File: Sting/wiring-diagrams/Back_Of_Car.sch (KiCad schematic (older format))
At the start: 34 parts, among them M1 Starter Motor, SW3 ExternalKill

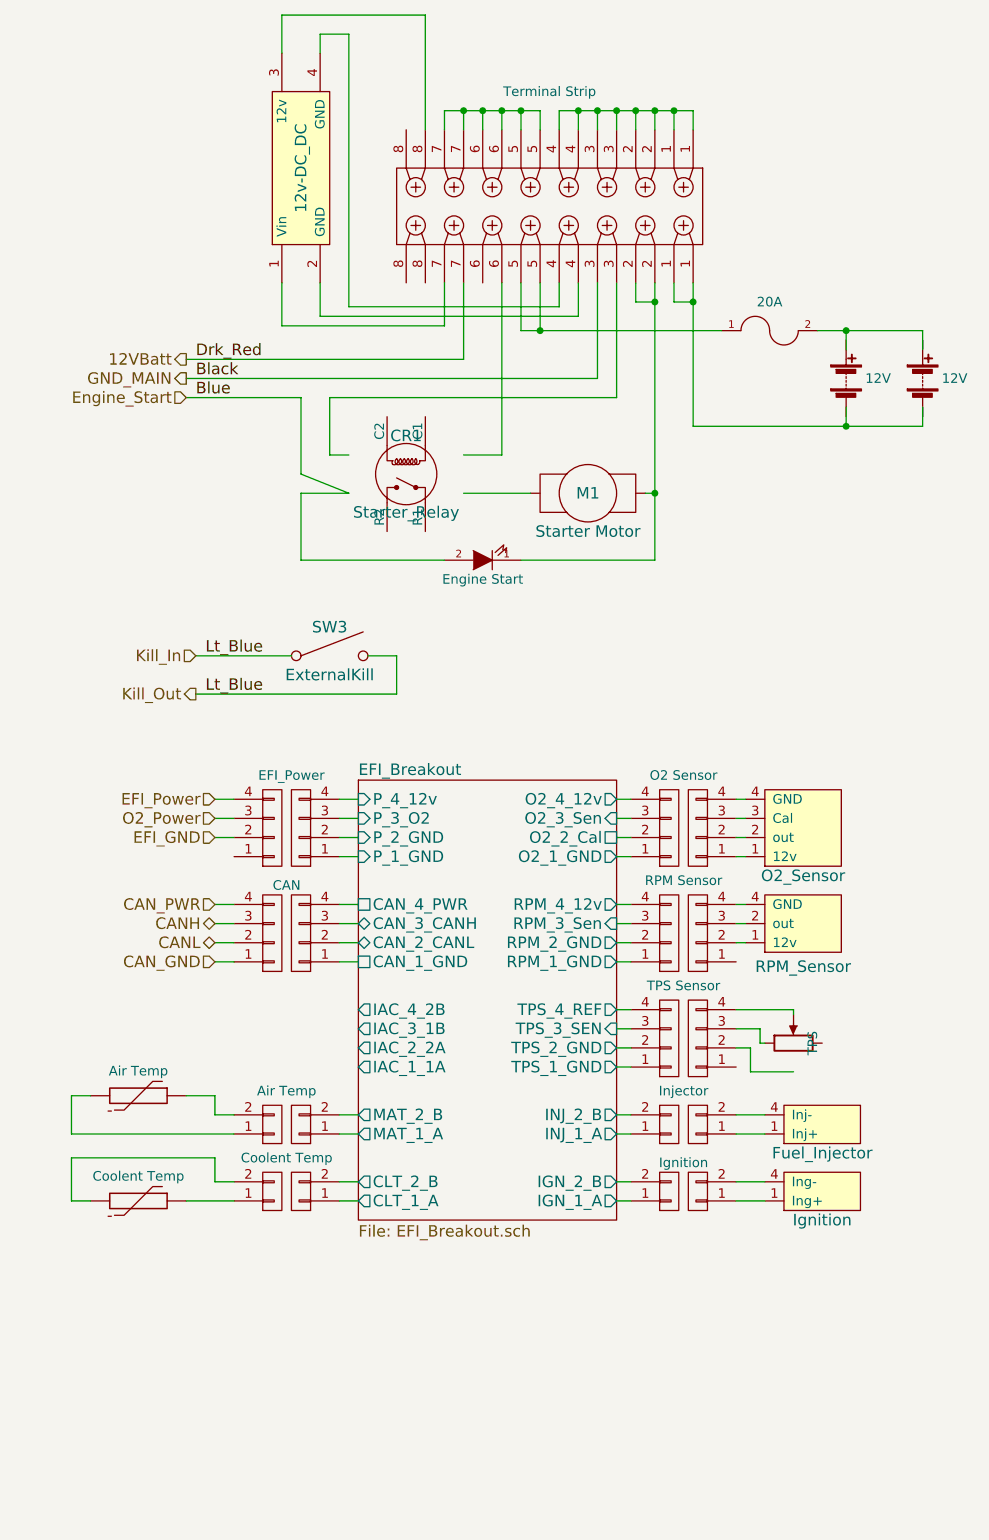
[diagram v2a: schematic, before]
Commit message: fixed missing parts updated sensor boards
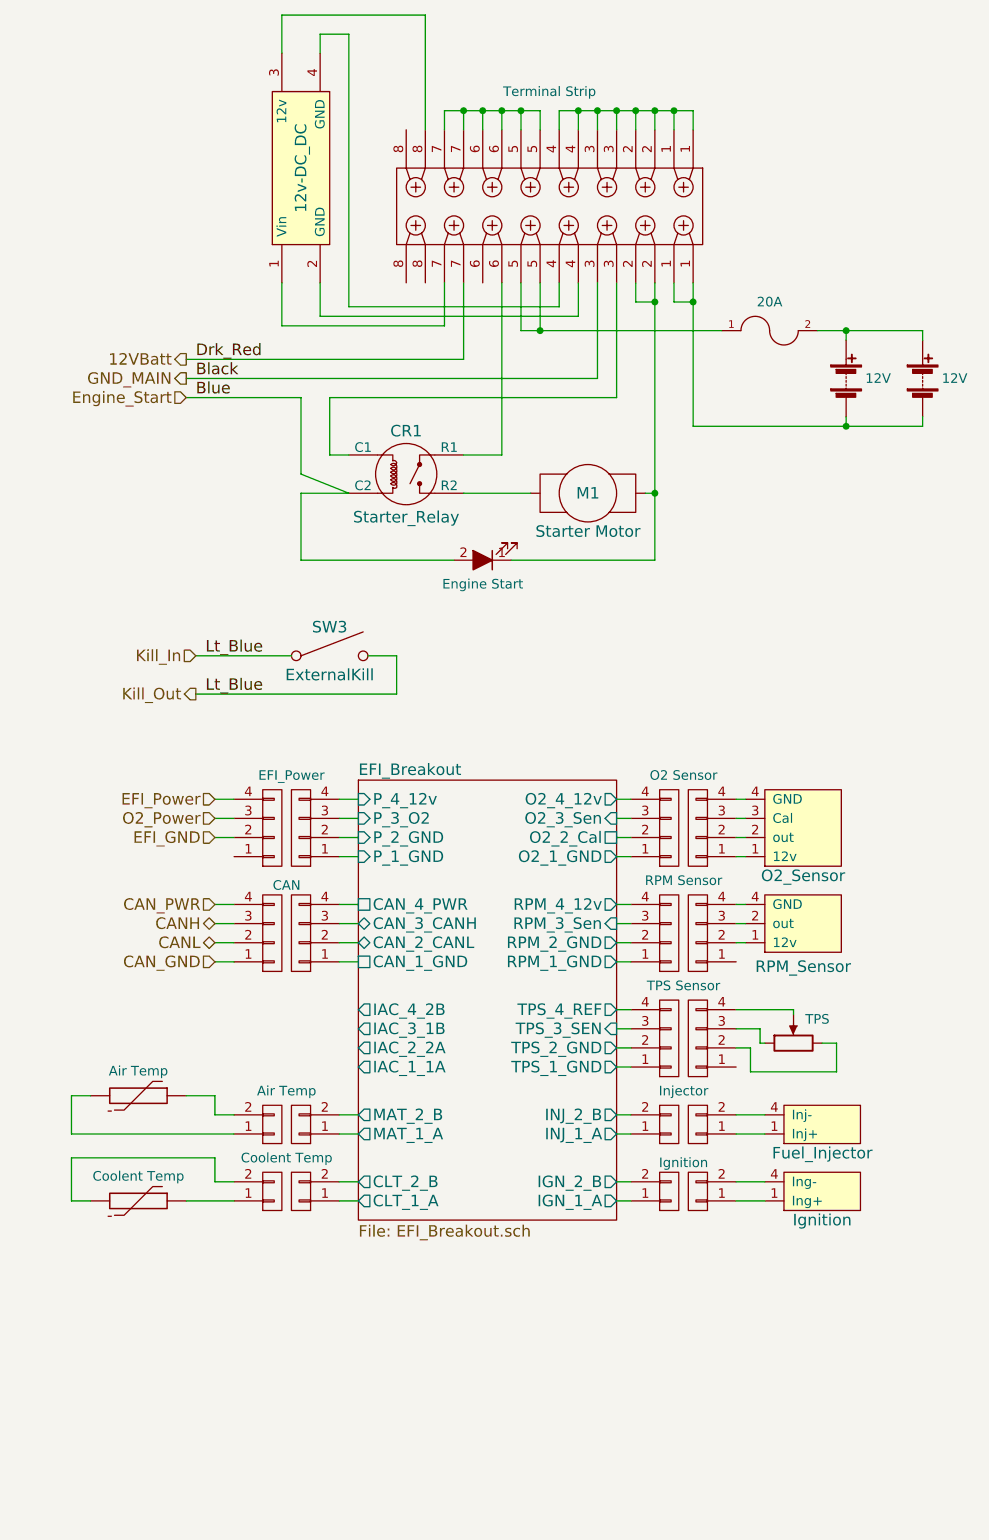
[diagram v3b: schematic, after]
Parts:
- removed D?: Engine Start, symbol LED
- added D?: Engine Start, symbol LED_ALT
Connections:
- wire segments 134 -> 152
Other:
- moved on the sheet: CR1
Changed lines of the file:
@@
 U 1 1 57E6F37B
 P 3975 3925
-F 0 "CR1" V 3775 3925 60  0000 C CNN
-F 1 "Starter_Relay" V 4175 3925 60  0000 C CNN
+F 0 "CR1" H 3975 4150 60  0000 C CNN
+F 1 "Starter_Relay" H 3975 3700 60  0000 C CNN
 F 2 "" H 3975 3925 60  0001 C CNN
 F 3 "" H 3975 3925 60  0001 C CNN
 	1    3975 3925
-	0    1    1    0
+	1    0    0    -1
 $EndComp
 Text HLabel 2825 3425 0    60   Output ~ 0
@@
 Text HLabel 2825 3325 0    60   Output ~ 0
 12VBatt
-$Comp
-L LED D?
-U 1 1 57E7BBBA
-P 4375 4375
-F 0 "D?" H 4375 4475 50  0001 C CNN
-F 1 "Engine Start" H 4375 4475 50  0000 C CNN
-F 2 "" H 4375 4375 50  0000 C CNN
-F 3 "" H 4375 4375 50  0000 C CNN
-	1    4375 4375
-	-1   0    0    1
-$EndComp
 Text HLabel 2825 3525 0    60   Input ~ 0
 Engine_Start
@@
 U 1 1 57E6F190
 P 6275 3425
+AR Path="/57E6F190" Ref="BT?"  Part="1"
+AR Path="/57E2AF30/57E6F190" Ref="BT?"  Part="1"
 F 0 "BT?" V 6075 3375 50  0001 L CNN
 F 1 "12V" H 6375 3425 50  0000 L CNN
@@
 U 1 1 5880064A
 P 6675 3425
+AR Path="/5880064A" Ref="BT?"  Part="1"
+AR Path="/57E2AF30/5880064A" Ref="BT?"  Part="1"
 F 0 "BT?" V 6475 3375 50  0001 L CNN
 F 1 "12V" H 6775 3425 50  0000 L CNN
@@
 U 1 1 5893DA3D
 P 6000 6900
-F 0 "TPS" H 6000 6800 50  0000 C CNN
+AR Path="/5893DA3D" Ref="TPS"  Part="1"
+AR Path="/57E2AF30/5893DA3D" Ref="TPS"  Part="1"
+F 0 "TPS" V 6125 6775 50  0000 C CNN
 F 1 "POT" H 6000 6900 50  0001 C CNN
 F 2 "" H 6000 6900 50  0000 C CNN
@@
 	5475 2025 5475 2125
 Wire Wire Line
-	4775 2025 5475 2025
+	4775 2025 4875 2025
+Wire Wire Line
+	4875 2025 4975 2025
+Wire Wire Line
+	4975 2025 5075 2025
+Wire Wire Line
+	5075 2025 5175 2025
+Wire Wire Line
+	5175 2025 5275 2025
+Wire Wire Line
+	5275 2025 5375 2025
+Wire Wire Line
+	5375 2025 5475 2025
 Wire Wire Line
 	5375 2025 5375 2125
@@
 Connection ~ 4475 2025
 Wire Wire Line
-	5475 3675 6675 3675
-Wire Wire Line
-	5475 2925 5475 3675
+	5475 3675 6275 3675
+Wire Wire Line
+	6275 3675 6675 3675
+Wire Wire Line
+	5475 2925 5475 3025
+Wire Wire Line
+	5475 3025 5475 3675
 Wire Wire Line
 	5375 2925 5375 3025
@@
 	2825 3525 3425 3525
 Wire Wire Line
-	5275 2925 5275 4375
+	5275 2925 5275 3025
+Wire Wire Line
+	5275 3025 5275 4025
+Wire Wire Line
+	5275 4025 5275 4375
 Wire Wire Line
 	5175 2925 5175 3025
@@
 	4675 3175 4675 2925
 Wire Wire Line
-	4175 2025 4675 2025
+	4175 2025 4275 2025
+Wire Wire Line
+	4275 2025 4375 2025
+Wire Wire Line
+	4375 2025 4475 2025
+Wire Wire Line
+	4475 2025 4575 2025
+Wire Wire Line
+	4575 2025 4675 2025
 Wire Wire Line
 	4775 2125 4775 2025
@@
 	5275 4025 5225 4025
 Wire Wire Line
-	4175 4375 3425 4375
+	4225 4375 3425 4375
 Wire Wire Line
 	3425 4375 3425 4025
@@
 	3425 4025 3675 4025
 Wire Wire Line
-	5275 4375 4575 4375
+	5275 4375 4525 4375
 Connection ~ 5275 4025
 Wire Wire Line
@@
 	3575 3825 3675 3825
 Wire Wire Line
-	6125 3175 6675 3175
-Wire Wire Line
-	4575 3175 5625 3175
-Wire Wire Line
-	6275 3675 6275 3575
-Wire Wire Line
-	6275 3275 6275 3175
-Wire Wire Line
-	6675 3175 6675 3275
+	6125 3175 6275 3175
+Wire Wire Line
+	6275 3175 6675 3175
+Wire Wire Line
+	4575 3175 4675 3175
+Wire Wire Line
+	4675 3175 5625 3175
+Wire Wire Line
+	6275 3675 6275 3625
+Wire Wire Line
+	6275 3225 6275 3175
+Wire Wire Line
+	6675 3175 6675 3225
 Connection ~ 6275 3175
 Wire Wire Line
-	6675 3675 6675 3575
+	6675 3675 6675 3625
 Connection ~ 6275 3675
 Wire Wire Line
@@
 	6000 6725 5700 6725
 Wire Wire Line
-	6000 7050 5775 7050
+	6225 7050 5775 7050
 Wire Wire Line
 	5775 7050 5775 6925
@@
 Wire Wire Line
 	4075 1525 4075 2125
+Wire Wire Line
+	6225 7050 6225 6900
+Wire Wire Line
+	6225 6900 6150 6900
+$Comp
+L LED_ALT D?
+U 1 1 58BFCDF3
+P 4375 4375
+F 0 "D?" H 4375 4475 50  0001 C CNN
+F 1 "Engine Start" H 4375 4500 50  0000 C CNN
+F 2 "" H 4375 4375 50  0000 C CNN
+F 3 "" H 4375 4375 50  0000 C CNN
+	1    4375 4375
+	-1   0    0    1
+$EndComp
 $EndSCHEMATC

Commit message: Moved where the relay to turn on the starter relay gets power from
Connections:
- net at P?.6: no longer CR1.~ (R2)
- net at P?.8: now also U?.3 (12v)
- new net: CR1.~ (R2), P?.3
- new net: CR1.~ (R2), P?.6
- new net: P?.5, P?.6, P?.7
- now unconnected: P?.6
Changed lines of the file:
@@
 EESchema Schematic File Version 2
+LIBS:Wiring Diagram v2-rescue
 LIBS:power
 LIBS:device

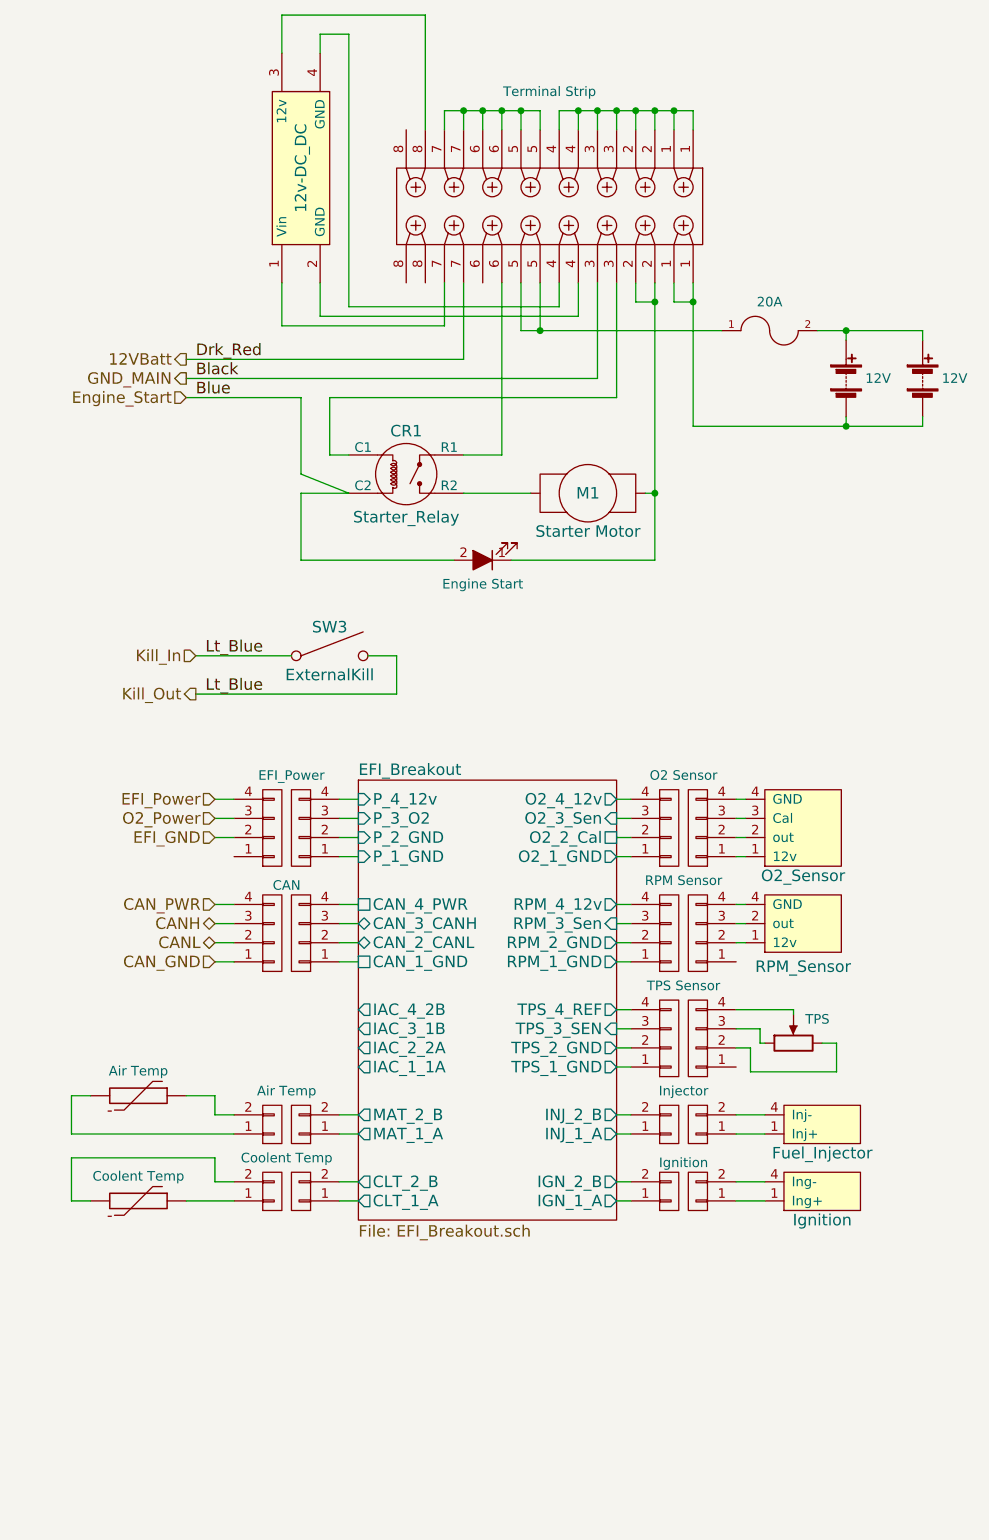
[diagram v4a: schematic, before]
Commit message: Added Canopy Switches to Sting Documentation
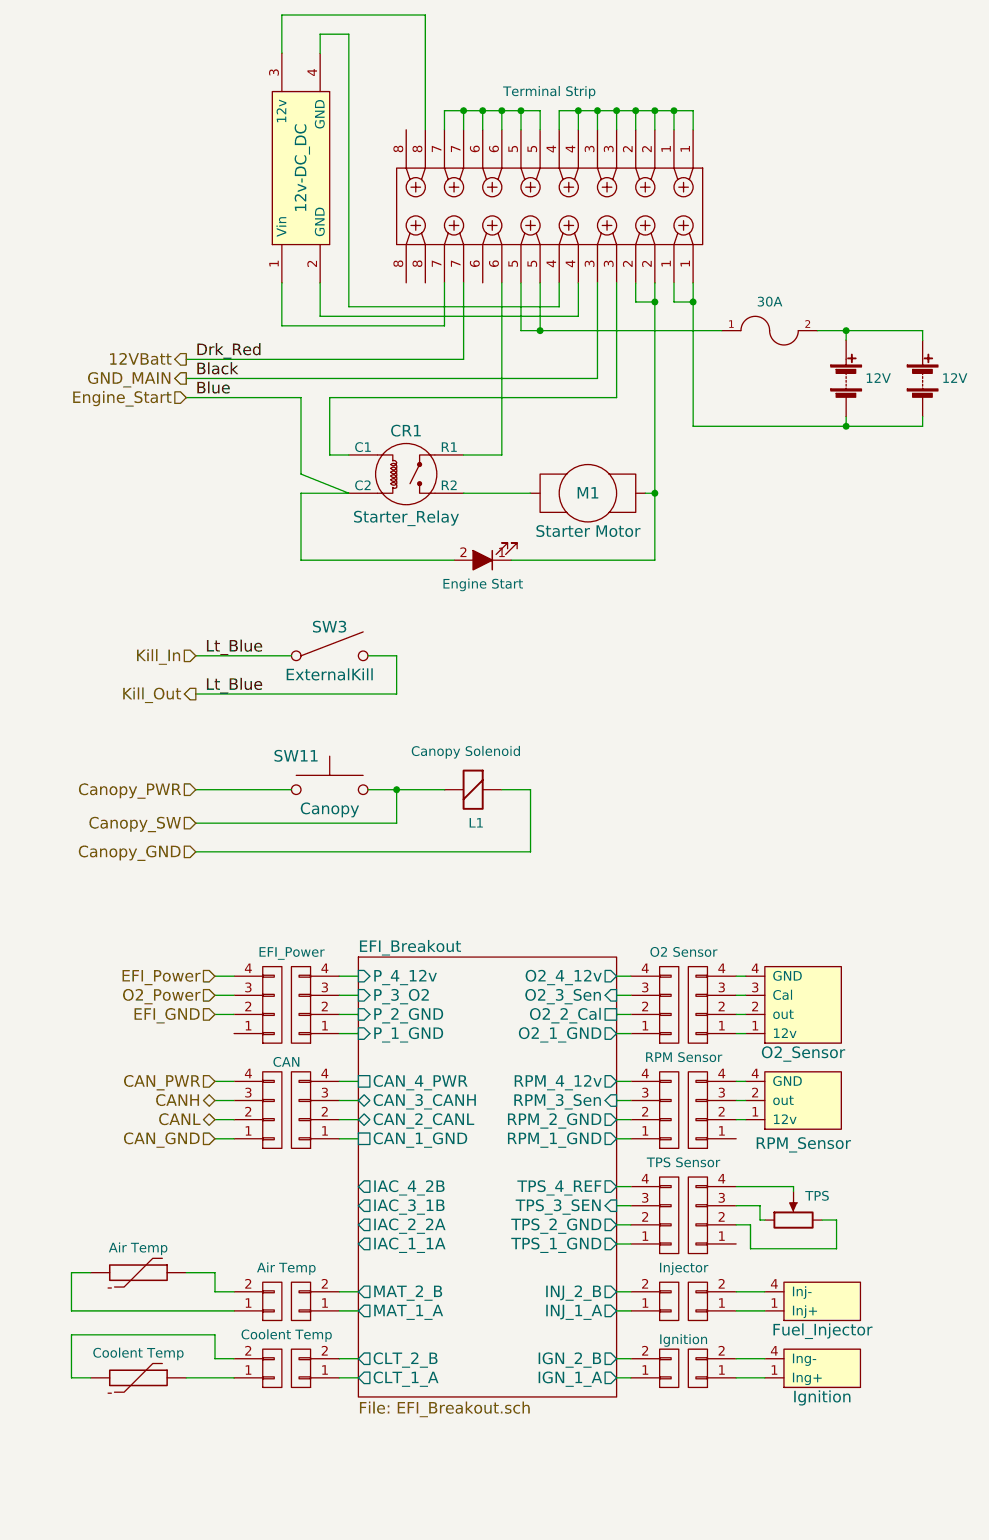
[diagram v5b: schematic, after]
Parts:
- added L1: Canopy Solenoid, symbol Electromagnetic_Actor
- added SW11: Canopy, symbol SW_Push
- F?: value 20A -> 30A
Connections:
- net at P?.6: no longer CR1.~ (R2)
- net at P?.8: now also U?.3 (12v)
- new net: CR1.~ (R2), P?.3
- new net: CR1.~ (R2), P?.6
- new net: P?.5, P?.6, P?.7
- new net Canopy_GND: L1.1 (-)
- new net Canopy_PWR: SW11.1
- new net Canopy_SW: L1.2 (+), SW11.2
- now unconnected: P?.6
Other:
- moved on the sheet: TPS
